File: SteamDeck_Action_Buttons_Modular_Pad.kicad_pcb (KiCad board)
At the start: 2 copper layers, 50.2 x 32.1 mm, 15 parts

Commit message: rev 0.2
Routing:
- net GND: track 86.4 -> 59.4 mm, vias 9 -> 12
- net Y-Button: track 58.6 -> 51.3 mm, vias 1 -> 3
- net Menu-Button: track 65.7 -> 68.6 mm, vias 1 -> 3
- net X-Button: track 47.9 -> 49.3 mm, vias 1 -> 3
- net A-Button: track 34.4 -> 34.9 mm, vias 1 -> 3
- net B-Button: track 35.5 -> 35.7 mm, vias 1 -> 3
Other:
- board text added: "Rev 0.2 M.Hourani"
- board text removed: "Rev 0.1 M.Hourani"

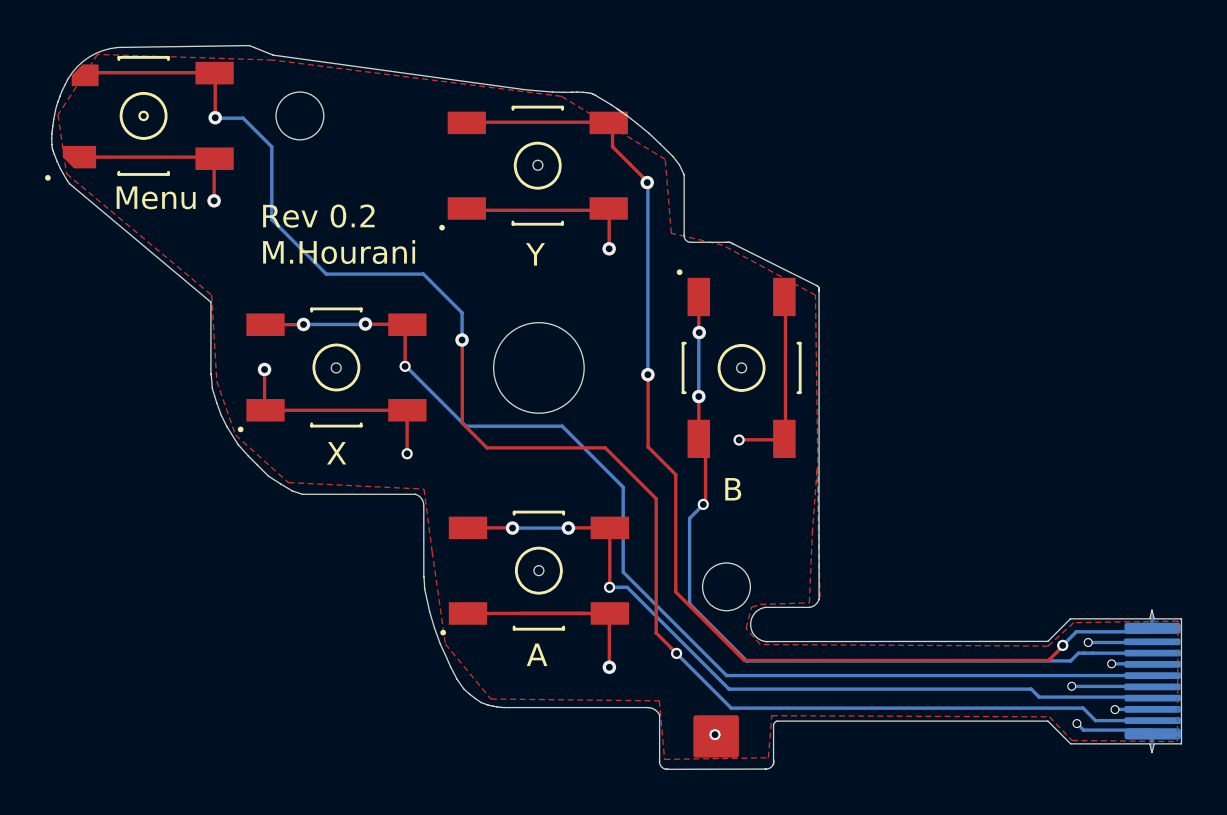
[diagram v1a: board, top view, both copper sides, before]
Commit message: Updated stiffener on board
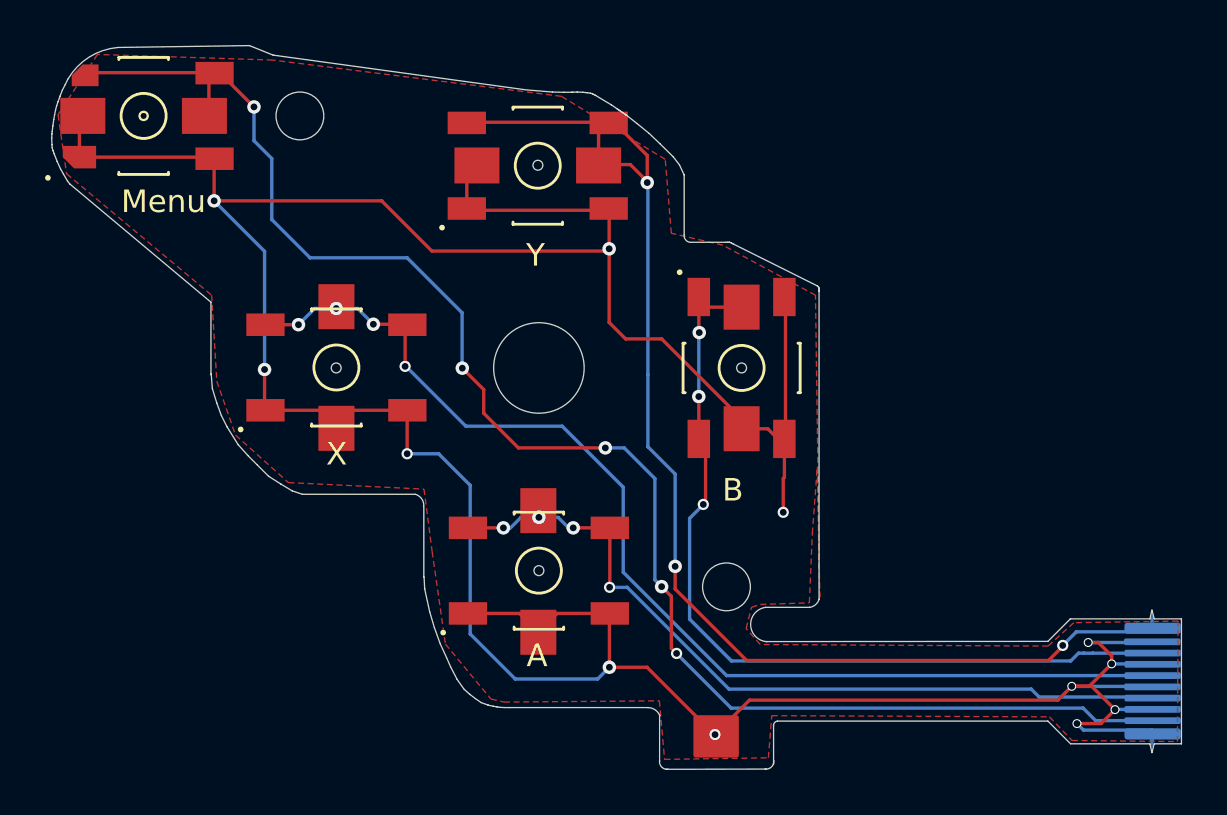
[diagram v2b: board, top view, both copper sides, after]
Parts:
- added REF**: SW_SPST_EVQPE1, Button_Switch_SMD:SW_SPST_EVQPE1, F.Cu at (150.1, 88.6)
- added REF**: SW_SPST_EVQPE1, Button_Switch_SMD:SW_SPST_EVQPE1, F.Cu at (141.2, 79.6)
- added REF**: SW_SPST_EVQPE1, Button_Switch_SMD:SW_SPST_EVQPE1, F.Cu at (150.1, 70.6)
- added REF**: SW_SPST_EVQPE1, Button_Switch_SMD:SW_SPST_EVQPE1, F.Cu at (159.2, 79.6)
- added REF**: SW_SPST_EVQPE1, Button_Switch_SMD:SW_SPST_EVQPE1, F.Cu at (132.6, 68.4)
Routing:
- net GND: track 59.4 -> 151.3 mm
- net Y-Button: track 51.3 -> 56.0 mm
- net B-Button: track 35.7 -> 38.2 mm
- net Menu-Button: track 68.6 -> 70.0 mm, vias 3 -> 5
- net A-Button: track 34.9 -> 35.6 mm, vias 3 -> 4
- net X-Button: track 49.3 -> 49.9 mm, vias 3 -> 4
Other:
- board text added: "Rev 0.3 M.Hourani"
- board text removed: "Rev 0.2 M.Hourani"
